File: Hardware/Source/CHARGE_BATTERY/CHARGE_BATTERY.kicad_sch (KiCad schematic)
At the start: 0 parts

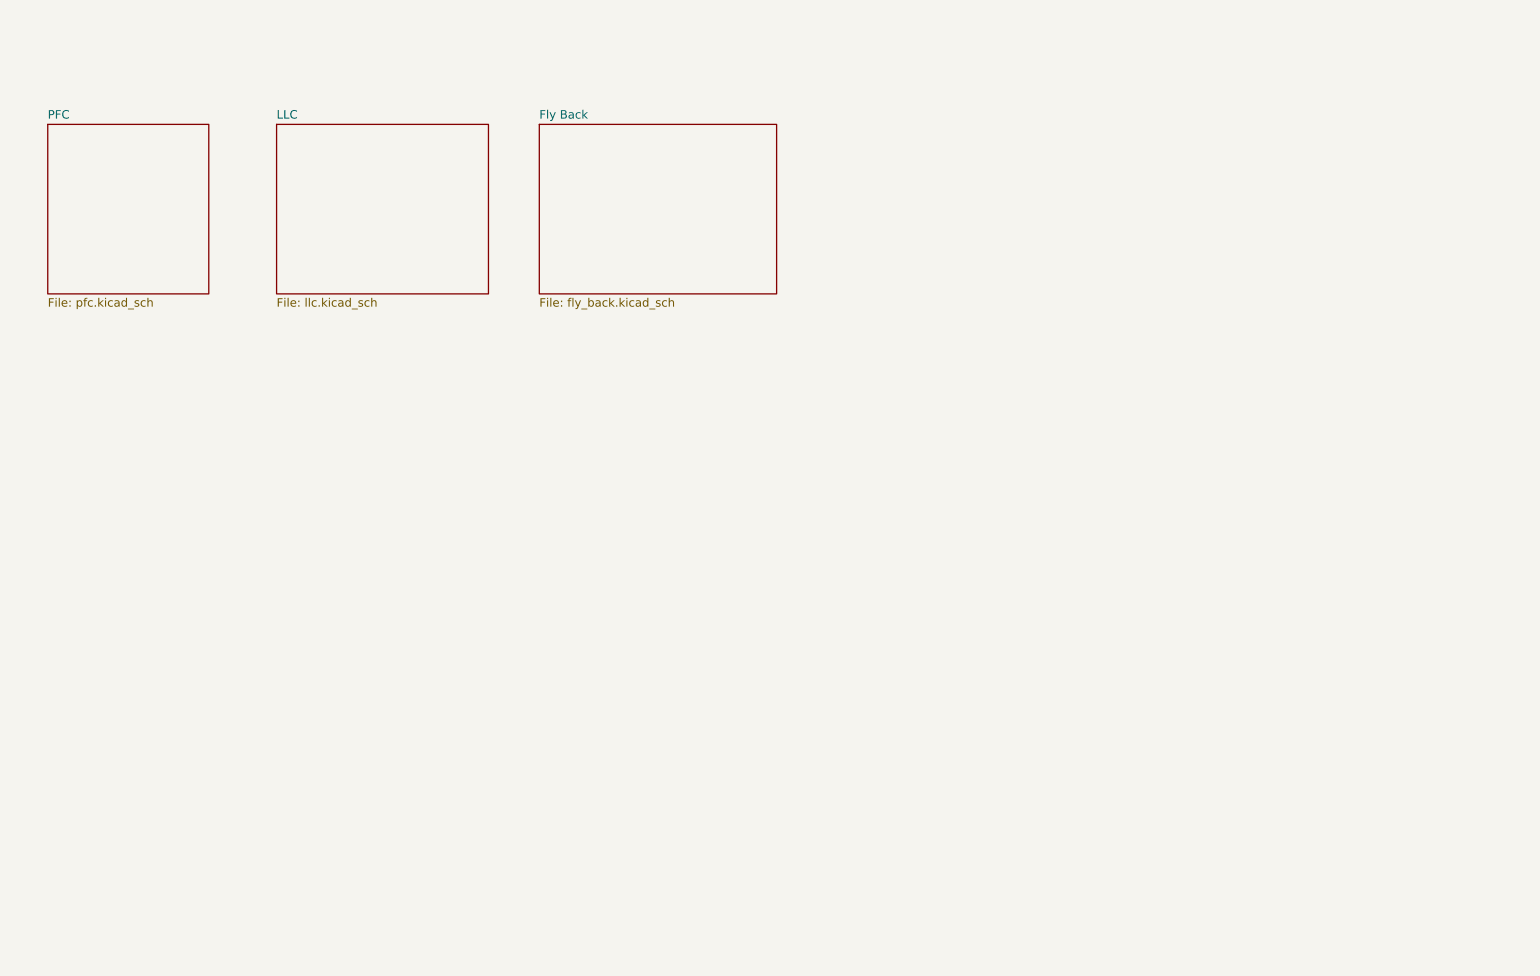
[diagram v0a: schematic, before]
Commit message: Add MCU Schematic, missing library components for MCU, not done
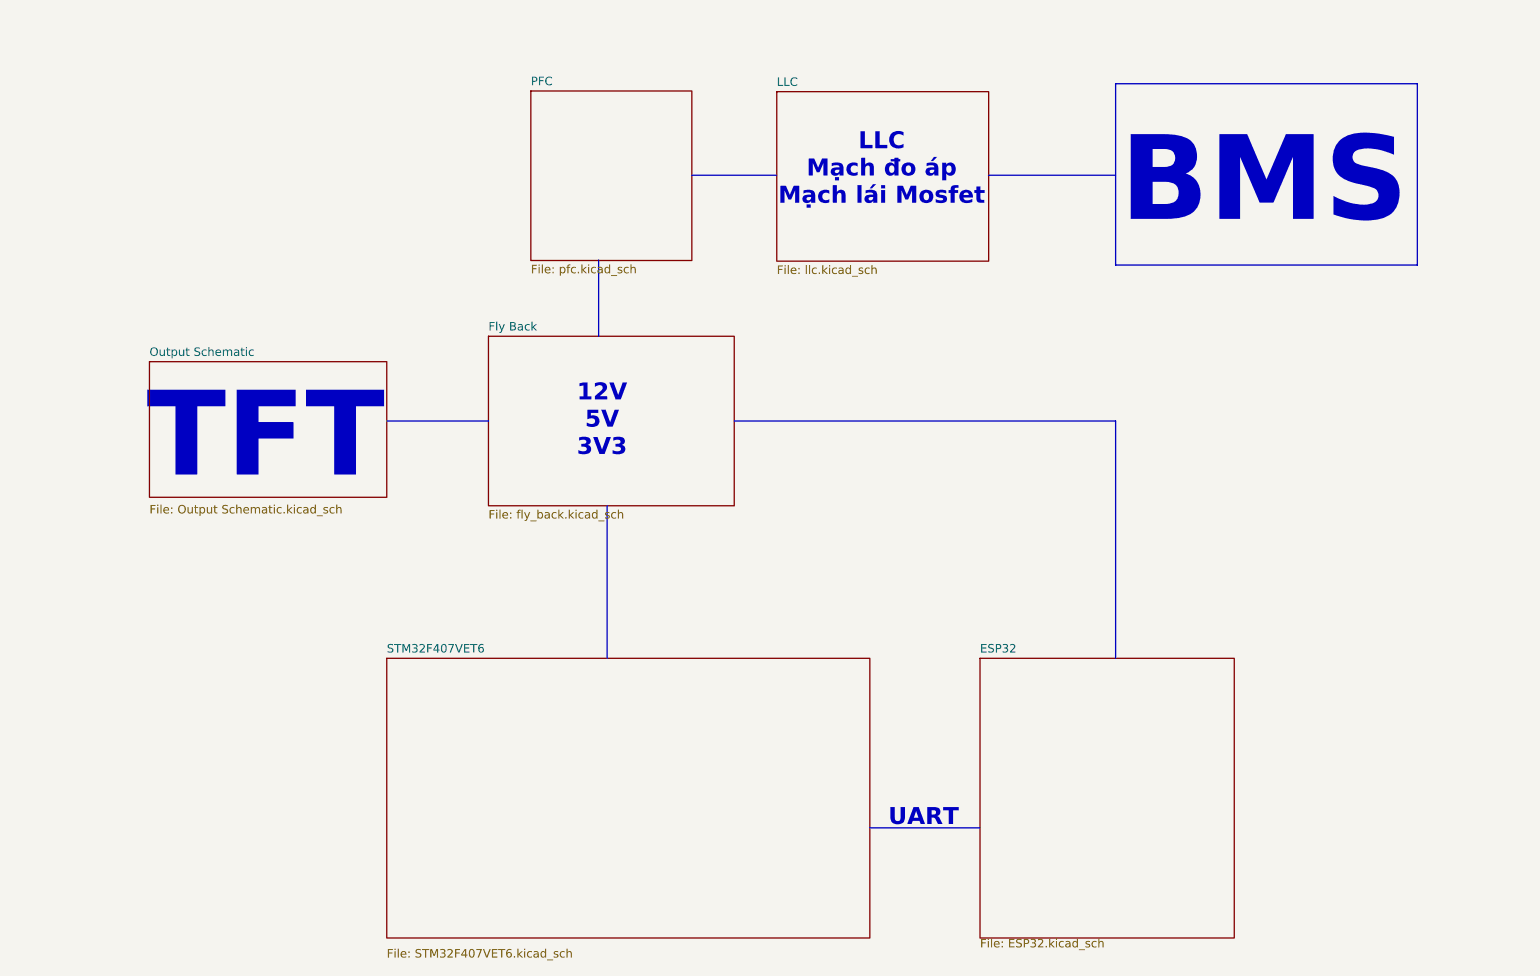
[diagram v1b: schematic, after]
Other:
- added sheet ESP32 (ESP32.kicad_sch)
- added sheet Output Schematic (Output Schematic.kicad_sch)
- added sheet STM32F407VET6 (STM32F407VET6.kicad_sch)
- note added: "12V 5V 3V3"
- note added: "BMS"
- note added: "LLC Mạch đo áp Mạch lái Mosfet"
- note added: "TFT"
- note added: "UART"

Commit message: Combine Sche in Source: PFC, LLC, F1, F4, ESP32
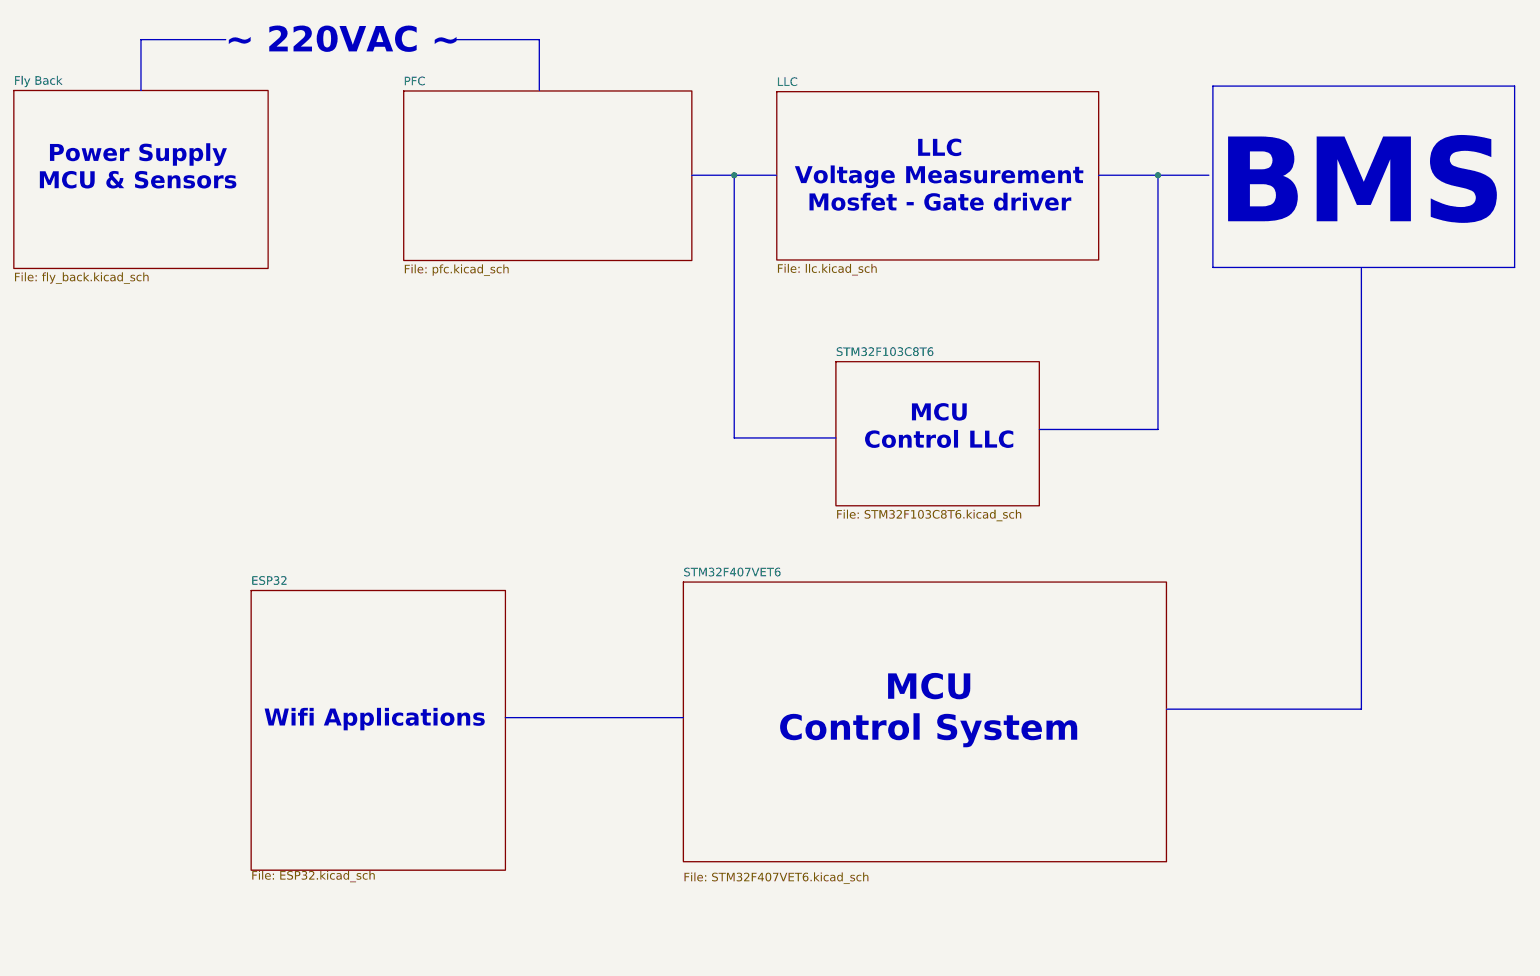
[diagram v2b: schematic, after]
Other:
- removed sheet Output Schematic
- added sheet STM32F103C8T6 (STM32F103C8T6.kicad_sch)
- note added: "LLC Voltage Measurement Mosfet - Gate driver"
- note added: "MCU Control LLC"
- note added: "MCU Control System"
- note added: "Power Supply MCU & Sensors"
- note added: "Wifi Applications"
- note added: "~ 220VAC ~"
- note removed: "12V 5V 3V3"
- note removed: "LLC Mạch đo áp Mạch lái Mosfet"
- note removed: "TFT"
- note removed: "UART"
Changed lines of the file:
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@@
 	(generator_version "8.0")
 	(paper "A4")
-	(bus
-		(pts
-			(xy 198.12 76.2) (xy 198.12 111.76)
-		)
-		(stroke
-			(width 0)
-			(type default)
-		)
-	)
-	(bus
-		(pts
-			(xy 134.62 39.37) (xy 147.32 39.37)
-		)
-		(stroke
-			(width 0)
-			(type default)
-		)
-	)
-	(bus
-		(pts
-			(xy 120.65 52.07) (xy 120.65 63.5)
-		)
-		(stroke
-			(width 0)
-			(type default)
-		)
-	)
-	(bus
-		(pts
-			(xy 140.97 76.2) (xy 198.12 76.2)
-		)
-		(stroke
-			(width 0)
-			(type default)
-		)
-	)
-	(bus
-		(pts
-			(xy 88.9 76.2) (xy 104.14 76.2)
-		)
-		(stroke
-			(width 0)
-			(type default)
-		)
-	)
-	(bus
-		(pts
-			(xy 121.92 88.9) (xy 121.92 111.76)
-		)
-		(stroke
-			(width 0)
-			(type default)
-		)
-	)
-	(bus
-		(pts
-			(xy 179.07 39.37) (xy 198.12 39.37)
-		)
-		(stroke
-			(width 0)
-			(type default)
-		)
-	)
-	(bus
-		(pts
-			(xy 161.29 137.16) (xy 177.8 137.16)
+	(junction
+		(at 204.47 39.37)
+		(diameter 0)
+		(color 0 0 0 0)
+	)
+	(junction
+		(at 140.97 39.37)
+		(diameter 0)
+		(color 0 0 0 0)
+	)
+	(bus
+		(pts
+			(xy 52.07 19.05) (xy 52.07 26.67)
+		)
+		(stroke
+			(width 0)
+			(type default)
+		)
+	)
+	(bus
+		(pts
+			(xy 204.47 39.37) (xy 204.47 77.47)
+		)
+		(stroke
+			(width 0)
+			(type dash)
+		)
+	)
+	(bus
+		(pts
+			(xy 99.06 19.05) (xy 111.76 19.05)
+		)
+		(stroke
+			(width 0)
+			(type default)
+		)
+	)
+	(bus
+		(pts
+			(xy 64.77 19.05) (xy 52.07 19.05)
+		)
+		(stroke
+			(width 0)
+			(type default)
+		)
+	)
+	(bus
+		(pts
+			(xy 140.97 78.74) (xy 140.97 39.37)
+		)
+		(stroke
+			(width 0)
+			(type default)
+		)
+	)
+	(bus
+		(pts
+			(xy 111.76 19.05) (xy 111.76 26.67)
+		)
+		(stroke
+			(width 0)
+			(type default)
+		)
+	)
+	(bus
+		(pts
+			(xy 140.97 39.37) (xy 147.32 39.37)
+		)
+		(stroke
+			(width 0)
+			(type default)
+		)
+	)
+	(bus
+		(pts
+			(xy 204.47 39.37) (xy 212.09 39.37)
+		)
+		(stroke
+			(width 0)
+			(type default)
+		)
+	)
+	(bus
+		(pts
+			(xy 186.69 77.47) (xy 204.47 77.47)
+		)
+		(stroke
+			(width 0)
+			(type dash)
+		)
+	)
+	(bus
+		(pts
+			(xy 106.68 120.65) (xy 133.35 120.65)
+		)
+		(stroke
+			(width 0)
+			(type default)
+		)
+	)
+	(bus
+		(pts
+			(xy 134.62 39.37) (xy 140.97 39.37)
+		)
+		(stroke
+			(width 0)
+			(type default)
+		)
+	)
+	(bus
+		(pts
+			(xy 205.74 119.38) (xy 234.95 119.38)
+		)
+		(stroke
+			(width 0)
+			(type default)
+		)
+	)
+	(bus
+		(pts
+			(xy 195.58 39.37) (xy 204.47 39.37)
+		)
+		(stroke
+			(width 0)
+			(type default)
+		)
+	)
+	(bus
+		(pts
+			(xy 234.95 53.34) (xy 234.95 119.38)
+		)
+		(stroke
+			(width 0)
+			(type default)
+		)
+	)
+	(bus
+		(pts
+			(xy 156.21 78.74) (xy 140.97 78.74)
 		)
 		(stroke
@@
 	)
 	(rectangle
-		(start 198.12 25.654)
-		(end 243.332 52.832)
+		(start 212.6996 26.0096)
+		(end 257.9116 53.1876)
 		(stroke
 			(width 0)
@@
 		)
 	)
+	(text "Wifi Applications"
+		(exclude_from_sim no)
+		(at 87.122 120.904 0)
+		(effects
+			(font
+				(size 2.54 2.54)
+				(bold yes)
+			)
+		)
+	)
 	(text "BMS"
 		(exclude_from_sim no)
-		(at 220.3704 40.2844 0)
+		(at 234.95 40.64 0)
 		(effects
 			(font
@@
 		)
 	)
-	(text "LLC\nMạch đo áp\nMạch lái Mosfet\n"
-		(exclude_from_sim no)
-		(at 163.068 38.481 0)
+	(text "MCU \nControl System"
+		(exclude_from_sim no)
+		(at 170.18 119.38 0)
+		(effects
+			(font
+				(size 3.81 3.81)
+				(bold yes)
+			)
+		)
+	)
+	(text "LLC\nVoltage Measurement\nMosfet - Gate driver\n"
+		(exclude_from_sim no)
+		(at 171.704 39.624 0)
 		(effects
 			(font
@@
 		)
 	)
-	(text "TFT"
-		(exclude_from_sim no)
-		(at 70.7644 78.5876 0)
-		(effects
-			(font
-				(size 12.7 12.7)
-				(bold yes)
-			)
-		)
-	)
-	(text "UART"
-		(exclude_from_sim no)
-		(at 169.3418 135.6614 0)
+	(text "MCU \nControl LLC"
+		(exclude_from_sim no)
+		(at 171.704 77.216 0)
 		(effects
 			(font
@@
 		)
 	)
-	(text "12V\n5V\n3V3"
-		(exclude_from_sim no)
-		(at 121.158 76.1238 0)
+	(text "Power Supply \nMCU & Sensors\n\n"
+		(exclude_from_sim no)
+		(at 51.562 40.386 0)
 		(effects
 			(font
@@
 		)
 	)
-	(sheet
-		(at 177.8 111.76)
+	(text "~ 220VAC ~"
+		(exclude_from_sim no)
+		(at 82.296 19.304 0)
+		(effects
+			(font
+				(size 3.81 3.81)
+				(thickness 0.762)
+				(bold yes)
+			)
+		)
+	)
+	(sheet
+		(at 68.58 101.6)
 		(size 38.1 41.91)
 		(fields_autoplaced yes)
@@
 		)
 		(property "Sheetname" "ESP32"
-			(at 177.8 111.0484 0)
+			(at 68.58 100.8884 0)
 			(effects
 				(font
@@
 		)
 		(property "Sheetfile" "ESP32.kicad_sch"
-			(at 177.8 153.7466 0)
+			(at 68.58 143.5866 0)
 			(effects
 				(font
@@
 	(sheet
 		(at 147.3454 26.8478)
-		(size 31.75 25.4)
+		(size 48.2346 25.2222)
 		(fields_autoplaced yes)
 		(stroke
@@
 		)
 		(property "Sheetfile" "llc.kicad_sch"
-			(at 147.3454 52.8324 0)
+			(at 147.3454 52.6546 0)
 			(effects
 				(font
@@
 	)
 	(sheet
-		(at 104.14 63.5)
-		(size 36.83 25.4)
+		(at 33.02 26.67)
+		(size 38.1 26.67)
 		(fields_autoplaced yes)
 		(stroke
@@
 		)
 		(property "Sheetname" "Fly Back"
-			(at 104.14 62.7884 0)
+			(at 33.02 25.9584 0)
 			(effects
 				(font
@@
 		)
 		(property "Sheetfile" "fly_back.kicad_sch"
-			(at 104.14 89.4846 0)
+			(at 33.02 53.9246 0)
 			(effects
 				(font
@@
 	)
 	(sheet
-		(at 110.49 26.7462)
-		(size 24.13 25.4)
+		(at 91.44 26.7462)
+		(size 43.18 25.4)
 		(fields_autoplaced yes)
 		(stroke
@@
 		)
 		(property "Sheetname" "PFC"
-			(at 110.49 26.0346 0)
+			(at 91.44 26.0346 0)
 			(effects
 				(font
@@
 		)
 		(property "Sheetfile" "pfc.kicad_sch"
-			(at 110.49 52.7308 0)
+			(at 91.44 52.7308 0)
 			(effects
 				(font
@@
 	)
 	(sheet
-		(at 53.34 67.31)
-		(size 35.56 20.32)
-		(fields_autoplaced yes)
-		(stroke
-			(width 0.1524)
-			(type solid)
-		)
-		(fill
-			(color 0 0 0 0.0000)
-		)
-		(property "Sheetname" "Output Schematic"
-			(at 53.34 66.5984 0)
-			(effects
-				(font
-					(size 1.27 1.27)
-				)
-				(justify left bottom)
-			)
-		)
-		(property "Sheetfile" "Output Schematic.kicad_sch"
-			(at 53.34 88.7226 0)
+		(at 156.21 67.31)
+		(size 30.48 21.59)
+		(fields_autoplaced yes)
+		(stroke
+			(width 0.1524)
+			(type solid)
+		)
+		(fill
+			(color 0 0 0 0.0000)
+		)
+		(property "Sheetname" "STM32F103C8T6"
+			(at 156.21 66.5984 0)
+			(effects
+				(font
+					(size 1.27 1.27)
+				)
+				(justify left bottom)
+			)
+		)
+		(property "Sheetfile" "STM32F103C8T6.kicad_sch"
+			(at 156.21 89.4846 0)
 			(effects
 				(font
@@
 	)
 	(sheet
-		(at 88.9 111.76)
+		(at 133.35 100.33)
 		(size 72.39 41.91)
 		(fields_autoplaced yes)
@@
 		)
 		(property "Sheetname" "STM32F407VET6"
-			(at 88.9 111.0484 0)
+			(at 133.35 99.6184 0)
 			(effects
 				(font
@@
 		)
 		(property "Sheetfile" "STM32F407VET6.kicad_sch"
-			(at 88.9 155.2706 0)
-			(effects
-				(font
+			(at 133.35 143.8406 0)
+			(effects
+				(font

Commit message: Hardware: Update PFC and Sheet Entry
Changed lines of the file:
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@@
+	(bus
+		(pts
+			(xy 80.01 21.59) (xy 80.01 82.55)
+		)
+		(stroke
+			(width 0)
+			(type dash)
+		)
+	)
 	(bus
 		(pts
@@
 		)
 	)
+	(bus
+		(pts
+			(xy 80.01 82.55) (xy 156.21 82.55)
+		)
+		(stroke
+			(width 0)
+			(type dash)
+		)
+	)
